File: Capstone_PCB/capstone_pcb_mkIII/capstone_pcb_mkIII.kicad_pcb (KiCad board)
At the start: 4 copper layers, 161.7 x 143.1 mm, 18 parts, among them J1 DISPLAY_HEADER, J2 UART_TX, J3 UART_RX, J4 GND, SW1 SW_Push, SW2 SW_Push, U1 TPS62125DSG

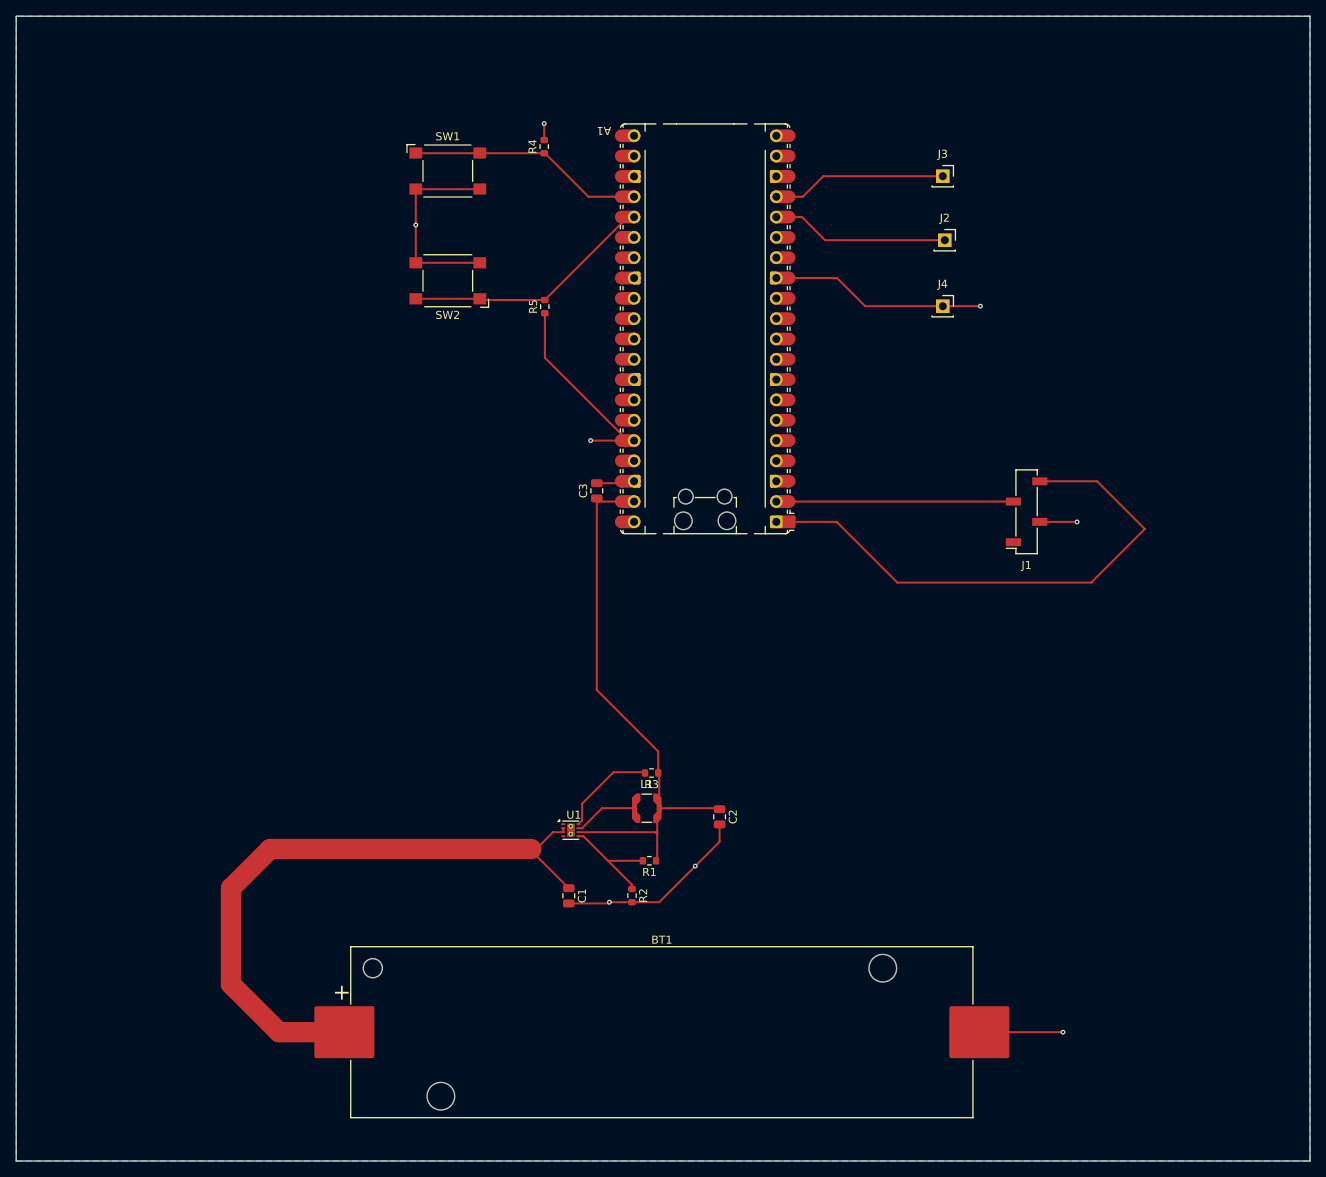
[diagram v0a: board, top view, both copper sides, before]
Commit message: pcb almost done, few more errors to iron out tomorrow
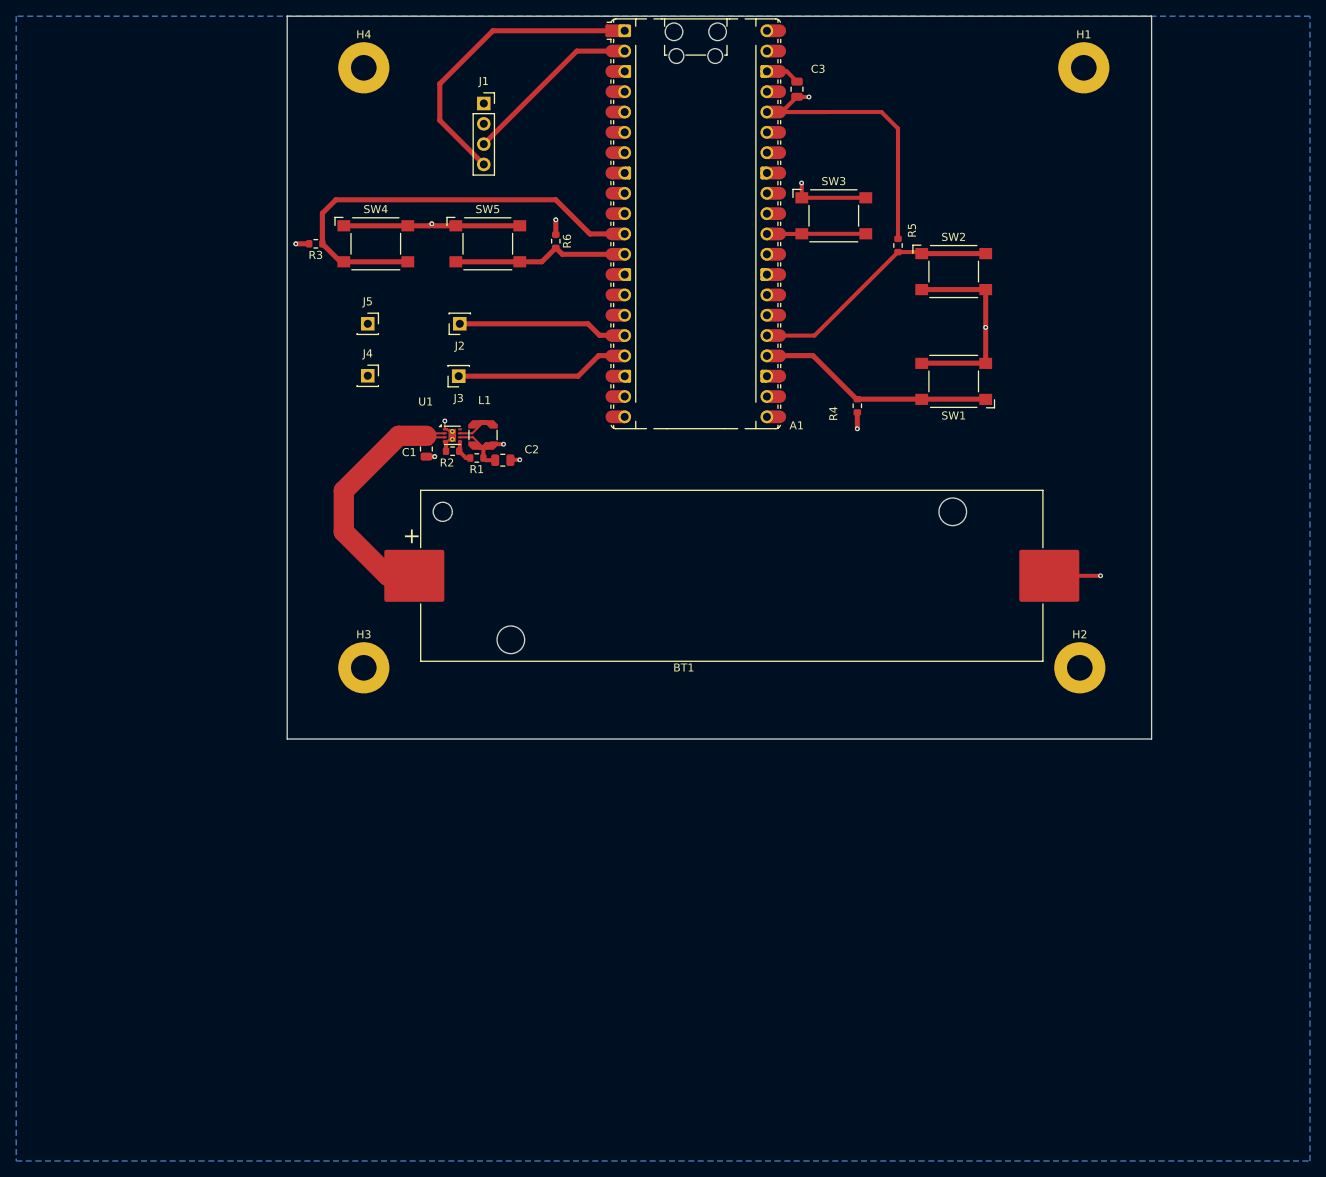
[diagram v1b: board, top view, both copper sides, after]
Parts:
- added H1: MountingHole_Pad, MountingHole:MountingHole_3.2mm_M3_Pad, F.Cu at (197.5, 27.5)
- added H2: MountingHole_Pad, MountingHole:MountingHole_3.2mm_M3_Pad, F.Cu at (197.0, 102.5)
- added H3: MountingHole_Pad, MountingHole:MountingHole_3.2mm_M3_Pad, F.Cu at (107.5, 102.5)
- added H4: MountingHole_Pad, MountingHole:MountingHole_3.2mm_M3_Pad, F.Cu at (107.5, 27.5)
- added J5: 3V3, Connector_PinSocket_2.54mm:PinSocket_1x01_P2.54mm_Vertical, F.Cu at (108.0, 59.5)
- added R6: 100kΩ, Resistor_SMD:R_0603_1608Metric, F.Cu at (131.5, 49.2)
- added SW3: SW_Push, Button_Switch_SMD:SW_SPST_Omron_B3FS-100xP, F.Cu at (166.2, 46.0)
- added SW4: SW_Push, Button_Switch_SMD:SW_SPST_Omron_B3FS-100xP, F.Cu at (109.0, 49.5)
- added SW5: SW_Push, Button_Switch_SMD:SW_SPST_Omron_B3FS-100xP, F.Cu at (123.0, 49.5)
- J1: footprint Connector_PinSocket_2.54mm:PinSocket_1x04_P2.54mm_Vertical_SMD_Pin1Right -> Connector_PinSocket_2.54mm:PinSocket_1x04_P2.54mm_Vertical
- R3: value 8kΩ -> 100kΩ
- moved J1 84.9 mm to (122.5, 32.0), turned to 0 degrees
- moved R3 78.3 mm to (101.5, 49.5)
- moved J4 72.4 mm to (108.0, 66.0)
- moved SW1 68.5 mm to (181.2, 66.7), turned to 180 degrees
- moved J3 65.5 mm to (119.4, 66.0), turned to 180 degrees
- moved SW2 63.2 mm to (181.2, 53.0), turned to 0 degrees
- moved J2 61.5 mm to (119.5, 59.5), turned to 180 degrees
- moved R2 59.9 mm to (118.6, 75.4), turned to 180 degrees
- moved C1 58.6 mm to (115.3, 75.2)
- moved BT1 57.7 mm to (153.5, 91.0)
- moved C3 56.1 mm to (161.7, 30.2)
- moved R1 54.8 mm to (121.6, 76.3)
- moved C2 52.2 mm to (124.9, 76.5), turned to 0 degrees
- moved U1 51.5 mm to (118.6, 73.4)
- moved L1 50.9 mm to (122.4, 73.4), turned to -90 degrees
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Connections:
- A1 pad 30: unconnected-(A1-RUN-Pad30) -> Net-(A1-RUN)
- A1 pad 37: unconnected-(A1-3V3_EN-Pad37) -> GND
- A1 pad 39: V_BC -> unconnected-(A1-VSYS-Pad39)_1
- J1 pad 1: Net-(A1-3V3) -> V_BC
- R3 pad 1: V_BC -> unconnected-(A1-GPIO8-Pad11)
- R3 pad 2: Net-(U1-PG) -> V_BC
- U1 pad 8: Net-(U1-PG) -> unconnected-(U1-PG-Pad8)
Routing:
- net unconnected-(A1-GPIO8-Pad11): track 0.00 -> 55.0 mm
- net Net-(BT1-+): track 80.4 -> 33.0 mm
- net V_BC: track 94.3 -> 50.1 mm, vias 2 -> 5
- net Net-(A1-GPIO0): track 66.8 -> 37.5 mm
- net unconnected-(A1-GPIO9-Pad12): track 0.00 -> 21.4 mm
- net GND: track 94.8 -> 74.2 mm, vias 6 -> 7
- net Net-(U1-PG): track 11.8 -> 0.00 mm
- net Net-(A1-RUN): track 0.00 -> 11.5 mm
- net Net-(U1-FB): track 14.1 -> 2.94 mm
- net Net-(A1-GPIO1): track 28.8 -> 21.7 mm
- net Net-(U1-SW): track 8.01 -> 3.44 mm
- net Net-(A1-GPIO19): track 30.8 -> 31.9 mm
- net Net-(A1-GPIO12): track 21.5 -> 20.9 mm
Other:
- board size 161.7 x 143.1 mm -> 108 x 90.4 mm

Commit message: new pcb
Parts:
- added R7: 0, Resistor_SMD:R_0603_1608Metric, F.Cu at (161.9, 29.2)
- added R8: 10k, Resistor_SMD:R_0603_1608Metric, F.Cu at (132.5, 22.9)
- added R9: 10k, Resistor_SMD:R_0603_1608Metric, F.Cu at (132.5, 26.0)
- moved C3 4.09 mm to (165.7, 30.2)
- moved R1 0.56 mm to (121.6, 76.8)
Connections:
- A1 pad 11: unconnected-(A1-GPIO8-Pad11) -> Net-(A1-GPIO8)
- A1 pad 12: unconnected-(A1-GPIO9-Pad12) -> Net-(A1-GPIO9)
- A1 pad 37: GND -> Net-(A1-3V3_EN)
- J1 pad 3: Net-(A1-GPIO1) -> Net-(J1-Pin_3)
- J1 pad 4: Net-(A1-GPIO0) -> Net-(J1-Pin_4)
- R3 pad 1: unconnected-(A1-GPIO8-Pad11) -> Net-(A1-GPIO8)
- R6 pad 2: unconnected-(A1-GPIO9-Pad12) -> Net-(A1-GPIO9)
- SW4 pad 2: unconnected-(A1-GPIO8-Pad11) -> Net-(A1-GPIO8)
- SW5 pad 2: unconnected-(A1-GPIO9-Pad12) -> Net-(A1-GPIO9)
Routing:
- net unconnected-(A1-GPIO8-Pad11): track 55.0 -> 0.00 mm
- net Net-(A1-GPIO8): track 0.00 -> 55.0 mm
- net Net-(A1-GPIO0): track 37.5 -> 5.96 mm
- net Net-(J1-Pin_4): track 0.00 -> 31.2 mm
- net V_BC: track 50.1 -> 23.3 mm
- net unconnected-(A1-GPIO9-Pad12): track 21.4 -> 0.00 mm
- net Net-(A1-GPIO9): track 0.00 -> 21.4 mm
- net Net-(A1-GPIO1): track 21.7 -> 6.22 mm
- net Net-(J1-Pin_3): track 0.00 -> 15.3 mm
- net Net-(A1-3V3_EN): track 0.00 -> 3.50 mm
- net Net-(U1-SW): track 3.44 -> 1.46 mm
- net GND: track 74.2 -> 75.1 mm, vias 7 -> 11
- added copper zone on F.Cu, net GND
